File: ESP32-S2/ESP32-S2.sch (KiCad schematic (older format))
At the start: 39 parts, among them J1 Conn_01x21_Male, J2 Conn_01x21_Male, J21 USB-C, Q1 L8050QLT1G, Q2 L8050QLT1G, SW1 BOOT/SELECT, SW2 EN/RESET, U1 ESP32-S2-WROOM, U2 SSD1306, U3 ATECC608A-SSHDA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

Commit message: resolved errors
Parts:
- C10, C9: value CP -> 1uF
- C11: value C_Small -> 10uF
- C6: value C_Small -> 1uF
- C7: value C_Small -> 0.1uF
- C8: value C_Small -> 2uF
- R5: value R_Small_US -> 390K
- R8: value R -> 4.7K
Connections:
- net labels added: VDD33, ~CTS, ~DTR
- net labels removed: CTS', DTR, DTR', Text Label 7420 2020 1    50   ~ 0
- wire segments 299 -> 286
- no-connect marks 6 -> 9
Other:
- moved on the sheet: C10, C9, R10, R6

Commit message: Some Changes in Schematic
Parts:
- removed U3: ATECC608A-SSHDA, Package_SO:SOIC-8_3.9x4.9mm_P1.27mm, symbol Security:ATECC608A-SSHDA
- added C9: C_Small, Capacitor_SMD:C_1206_3216Metric, symbol Device:C_Small
- added D4: 1N5819, Diode_THT:D_DO-41_SOD81_P10.16mm_Horizontal, symbol Diode:1N5819
- added J3: USB_A, symbol Connector:USB_A
- added Q1: DMP3013SFV, Package_SON:Diodes_PowerDI3333-8, symbol Transistor_FET:DMP3013SFV
- added R10: 220, Resistor_SMD:R_0603_1608Metric, symbol Device:R_Small_US
- added R11, R5, R8: 10K, Resistor_SMD:R_0603_1608Metric, symbol Device:R
- added R9: 100, Resistor_SMD:R_0603_1608Metric, symbol Device:R_Small_US
- added U3: LM1117-3.3, symbol Regulator_Linear:LM1117-3.3
- C1: renamed from C4; footprint (none) -> Capacitor_SMD:C_1206_3216Metric
- C10: renamed from C3; footprint (none) -> Capacitor_SMD:C_1206_3216Metric
- C11: renamed from C1; footprint (none) -> Capacitor_SMD:C_1206_3216Metric
- C12, C13, C5: footprint (none) -> Capacitor_SMD:C_1206_3216Metric
- C14: renamed from C2; footprint (none) -> Capacitor_SMD:C_1206_3216Metric
- C2: renamed from C6; footprint (none) -> Capacitor_SMD:C_1206_3216Metric
- C3: renamed from C7; footprint (none) -> Capacitor_SMD:C_1206_3216Metric
- C4: renamed from C8; footprint (none) -> Capacitor_SMD:C_1206_3216Metric
- C6: renamed from C9; footprint (none) -> Capacitor_SMD:C_1206_3216Metric
- C7: renamed from C10; footprint (none) -> Capacitor_SMD:C_1206_3216Metric
- C8: renamed from C11; footprint (none) -> Capacitor_SMD:C_1206_3216Metric
- D2, D3: footprint (none) -> LED_SMD:LED_0603_1608Metric_Castellated
- J2: footprint Connector_PinHeader_2.00mm:PinHeader_1x07_P2.00mm_Vertical -> Connector_PinHeader_2.00mm:PinHeader_1x21_P2.00mm_Vertical
- Q2: renamed from Q1; footprint (none) -> Button_Switch_SMD:SW_Push_1P1T_NO_6x6mm_H9.5mm
- Q3: renamed from Q2; footprint (none) -> Button_Switch_SMD:SW_Push_1P1T_NO_6x6mm_H9.5mm
- R1: renamed from R5; footprint (none) -> Resistor_SMD:R_0603_1608Metric
- R12: renamed from R9; footprint (none) -> Resistor_SMD:R_0603_1608Metric
- R13: renamed from R10; footprint (none) -> Resistor_SMD:R_0603_1608Metric
- R14: renamed from R3; footprint (none) -> Resistor_SMD:R_0603_1608Metric
- R15: renamed from R1; footprint (none) -> Resistor_SMD:R_0603_1608Metric
- R16: renamed from R2; footprint (none) -> Resistor_SMD:R_0603_1608Metric
- R17: renamed from R4; footprint (none) -> Resistor_SMD:R_0603_1608Metric
- R2: renamed from R6; footprint (none) -> Resistor_SMD:R_0603_1608Metric
- R3: renamed from R7; footprint (none) -> Resistor_SMD:R_0603_1608Metric
- R4: renamed from R8; footprint (none) -> Resistor_SMD:R_0603_1608Metric
- R6: renamed from R11; footprint (none) -> Resistor_SMD:R_0603_1608Metric
- R7: renamed from R12; footprint (none) -> Resistor_SMD:R_0603_1608Metric
- U2: renamed from U1; footprint XCVR_ESP32-S2-WROOM -> RF_Module:ESP32-WROOM-32
- renumbered J21 to J4, SW2 to SW1, SW1 to SW2, U2 to U1
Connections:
- net labels added: +BATT, VBUS, ~RTS
- net labels removed: RTS, SHLD, ~CTS
- wire segments 286 -> 320
- no-connect marks 9 -> 7
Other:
- moved on the sheet: C10, C11, C12, C13, C14, D2, D3, J4, Q2, Q3, R12, R13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

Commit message: made suggested changes
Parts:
- removed U3: LM1117-3.3, symbol Regulator_Linear:LM1117-3.3
- added TP1: GND, symbol Connector:TestPoint
- added TP2: 3V3, symbol Connector:TestPoint
- added TP3: SCL, symbol Connector:TestPoint
- added TP4: SDA, symbol Connector:TestPoint
- added U3: AMS1117-3.3, Package_TO_SOT_SMD:SOT-223-3_TabPin2, symbol Regulator_Linear:AMS1117-3.3
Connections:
- net +3V3: now also TP2.1, U3.2 (VO)
- net GND: now also TP1.1
- net SCL: now also R2.1, TP3.1; no longer R3.1
- net SDA: now also R3.1, TP4.1; no longer R2.1
- net RES#: now reaches C8.1, D1.2 (A), R4.2, U1.14 (RES#)
- net at D4.2 (A), Q1.1 (S), Q1.2 (S)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: now also U3.3 (VI)
- net at R10.1, R9.2: now also U3.1 (GND)
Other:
- note added: "Test Points\n"
- note added: "USB-A Voltage Divider\n\n"
- note added: "USB-C to UART\n"
- note removed: "USB and CH340C"
- note removed: "Voltage Divider\n"
- moved on the sheet: C10, C11, C8, C9, D1, D4, J2, Q1, R10, R11, R2, R3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

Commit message: Made changes in schematics
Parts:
- removed C9: C_Small, Capacitor_SMD:C_1206_3216Metric, symbol Device:C_Small
- removed R10: 220, Resistor_SMD:R_0603_1608Metric, symbol Device:R_Small_US
- removed R9: 100, Resistor_SMD:R_0603_1608Metric, symbol Device:R_Small_US
- removed U3: AMS1117-3.3, Package_TO_SOT_SMD:SOT-223-3_TabPin2, symbol Regulator_Linear:AMS1117-3.3
- added C15, C9, C?: 10uF, symbol Device:C
- added C?: 0.1uF, symbol Device:C
- added L1: 2.2uH, symbol Device:L
- added R?: R, symbol Device:R
- added U3: TPS63001, Package_SON:Texas_DRC0010J_ThermalVias, symbol Regulator_Switching:TPS63001
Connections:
- net GND: now also C15.2, C9.2, C?.2, C?.2, U3.11 (PGND), U3.3 (PGND), U3.9 (GND)
- new net: C15.1, C?.1, U3.1 (VOUT), U3.10 (FB)
- new net: L1.2, U3.2 (L2)
- new net: L1.1, U3.4 (L1)
- new net: R?.1, U3.5 (VIN)
- new net: C?.1, R?.2, U3.6 (EN), U3.7 (PS/SYNC), U3.8 (VINA)

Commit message: minor changes
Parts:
- R9: renamed from R?; value R -> 100
- gave numbers to parts that had none: 2
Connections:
- net +3V3: now also C15.1, C17.1, U3.1 (VOUT), U3.10 (FB)
- net at C9.1: now also D4.2 (A), Q1.1 (S), Q1.2 (S), Q1.3 (S)
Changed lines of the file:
@@
 Wire Notes Line
 	6970 7790 6970 5880
-Wire Notes Line
-	500  5880 6970 5880
 Text Notes 1325 725  0    93   ~ 0
 RF-Module
@@
 Wire Notes Line
 	2815 4060 2815 5905
-Wire Notes Line
-	2815 5905 2765 5905
 Wire Wire Line
 	2975 5130 2975 5225
@@
 	1    4660 5245
 	1    0    0    -1
-$EndComp
-$Comp
-L Device:R R11
-U 1 1 60557FF9
-P 4340 5505
-F 0 "R11" V 4430 5460 50  0000 L CNN
-F 1 "10K" V 4240 5435 50  0000 L CNN
-F 2 "Resistor_SMD:R_0603_1608Metric" V 4270 5505 50  0001 C CNN
-F 3 "~" H 4340 5505 50  0001 C CNN
-	1    4340 5505
-	-1   0    0    1
 $EndComp
 $Comp
@@
 Wire Notes Line
 	2095 7800 4370 7800
-Text Notes 3020 4430 0    118  ~ 0
-USB-A          Voltage Divider\n\n
-$Comp
-L Regulator_Switching:TPS63001 U3
-U 1 1 602467D8
-P 6300 4900
-F 0 "U3" H 6300 5567 50  0000 C CNN
-F 1 "TPS63001" H 6300 5476 50  0000 C CNN
-F 2 "Package_SON:Texas_DRC0010J_ThermalVias" H 7150 4350 50  0001 C CNN
-F 3 "http://www.ti.com/lit/ds/symlink/tps63000.pdf" H 6000 5450 50  0001 C CNN
-	1    6300 4900
-	1    0    0    -1
-$EndComp
-$Comp
-L Device:C C15
-U 1 1 6024B0B6
-P 6900 4950
-F 0 "C15" H 7015 4996 50  0000 L CNN
-F 1 "10uF" H 7015 4905 50  0000 L CNN
-F 2 "" H 6938 4800 50  0001 C CNN
-F 3 "~" H 6900 4950 50  0001 C CNN
-	1    6900 4950
-	1    0    0    -1
-$EndComp
-$Comp
-L Device:L L1
-U 1 1 6024B4E6
-P 6250 4200
-F 0 "L1" V 6440 4200 50  0000 C CNN
-F 1 "2.2uH" V 6349 4200 50  0000 C CNN
-F 2 "" H 6250 4200 50  0001 C CNN
-F 3 "~" H 6250 4200 50  0001 C CNN
-	1    6250 4200
-	0    -1   -1   0
-$EndComp
-Wire Wire Line
-	6100 4200 5800 4200
-Wire Wire Line
-	5800 4200 5800 4500
-Wire Wire Line
-	5800 4500 5900 4500
-Wire Wire Line
-	6400 4200 6850 4200
-Wire Wire Line
-	6850 4500 6700 4500
-Wire Wire Line
-	6850 4200 6850 4500
-$Comp
-L Device:C C9
-U 1 1 6024A509
-P 5650 5550
-F 0 "C9" H 5765 5596 50  0000 L CNN
-F 1 "10uF" H 5765 5505 50  0000 L CNN
-F 2 "" H 5688 5400 50  0001 C CNN
-F 3 "~" H 5650 5550 50  0001 C CNN
-	1    5650 5550
-	1    0    0    -1
-$EndComp
-Wire Wire Line
-	9150 3100 9250 3100
 Wire Notes Line
 	7450 5900 6950 5900
-Wire Wire Line
-	5650 5400 5650 5250
-Wire Wire Line
-	6700 4700 6750 4700
-Wire Wire Line
-	7200 5100 7200 5700
-Wire Wire Line
-	7200 5700 6900 5700
-Wire Wire Line
-	6900 5100 6900 5700
-Connection ~ 6900 5700
-Wire Wire Line
-	6900 5700 6550 5700
-Wire Wire Line
-	6200 5500 6200 5700
-Connection ~ 6200 5700
-Wire Wire Line
-	6200 5700 5800 5700
-Wire Wire Line
-	6300 5500 6300 5700
-Connection ~ 6300 5700
-Wire Wire Line
-	6300 5700 6200 5700
-Wire Wire Line
-	5000 5250 5650 5250
-Wire Wire Line
-	6700 4900 6750 4900
-Wire Wire Line
-	6750 4900 6750 4700
-Connection ~ 6750 4700
-Wire Wire Line
-	6750 4700 6900 4700
 $Comp
 L power:+3.3V #PWR011
@@
 	0    -1   -1   0
 $EndComp
-Wire Wire Line
-	6900 4700 6900 4800
-$Comp
-L Device:C C?
+Wire Notes Line
+	7450 4050 7450 5900
+Wire Notes Line
+	505  5905 6975 5905
+$Comp
+L Device:R R11
+U 1 1 60557FF9
+P 4340 5505
+F 0 "R11" H 4405 5435 50  0000 L CNN
+F 1 "10K" H 4410 5545 50  0000 L CNN
+F 2 "Resistor_SMD:R_0603_1608Metric" V 4270 5505 50  0001 C CNN
+F 3 "~" H 4340 5505 50  0001 C CNN
+	1    4340 5505
+	-1   0    0    1
+$EndComp
+Connection ~ 7200 4700
+Wire Wire Line
+	6900 4700 7200 4700
+$Comp
+L power:+3.3V #PWR030
+U 1 1 60EFC8D8
+P 7200 4700
+F 0 "#PWR030" H 7200 4550 50  0001 C CNN
+F 1 "+3.3V" H 7215 4873 50  0000 C CNN
+F 2 "" H 7200 4700 50  0001 C CNN
+F 3 "" H 7200 4700 50  0001 C CNN
+	1    7200 4700
+	1    0    0    -1
+$EndComp
+Wire Wire Line
+	5900 4900 5900 5100
+Connection ~ 5900 4900
+Connection ~ 5900 5100
+Wire Wire Line
+	5900 4800 5900 4900
+Wire Wire Line
+	5800 5100 5800 5150
+Connection ~ 5800 5100
+Wire Wire Line
+	5900 5100 5800 5100
+Wire Wire Line
+	5800 5700 5650 5700
+Connection ~ 5800 5700
+Wire Wire Line
+	5800 5450 5800 5700
+Wire Wire Line
+	5800 5050 5800 5100
+Wire Wire Line
+	5800 4700 5800 4750
+Wire Wire Line
+	5900 4700 5800 4700
+Connection ~ 6900 4700
+Wire Wire Line
+	7200 4700 7200 4800
+$Comp
+L Device:R R9
+U 1 1 60DDB77B
+P 5800 4900
+F 0 "R9" H 5650 4965 50  0000 L CNN
+F 1 "100" H 5610 4870 50  0000 L CNN
+F 2 "" V 5730 4900 50  0001 C CNN
+F 3 "~" H 5800 4900 50  0001 C CNN
+	1    5800 4900
+	1    0    0    -1
+$EndComp
+Wire Wire Line
+	6550 5700 6300 5700
+Connection ~ 6550 5700
+$Comp
+L power:GND #PWR025
+U 1 1 60D216C3
+P 6550 5700
+F 0 "#PWR025" H 6550 5450 50  0001 C CNN
+F 1 "GND" H 6550 5550 50  0000 C CNN
+F 2 "" H 6550 5700 50  0001 C CNN
+F 3 "" H 6550 5700 50  0001 C CNN
+	1    6550 5700
+	1    0    0    -1
+$EndComp
+$Comp
+L Device:C C17
+U 1 1 60D210CD
+P 7200 4950
+F 0 "C17" H 7270 5040 50  0000 L CNN
+F 1 "10uF" H 7255 4860 50  0000 L CNN
+F 2 "" H 7238 4800 50  0001 C CNN
+F 3 "~" H 7200 4950 50  0001 C CNN
+	1    7200 4950
+	1    0    0    -1
+$EndComp
+$Comp
+L Device:C C16
 U 1 1 60D204A0
 P 5800 5300
-F 0 "C?" H 5915 5346 50  0000 L CNN
-F 1 "0.1uF" H 5915 5255 50  0000 L CNN
+F 0 "C16" H 5835 5395 50  0000 L CNN
+F 1 "0.1uF" H 5795 5220 50  0000 L CNN
 F 2 "" H 5838 5150 50  0001 C CNN
 F 3 "~" H 5800 5300 50  0001 C CNN
@@
 	1    0    0    -1
 $EndComp
-$Comp
-L Device:C C?
-U 1 1 60D210CD
-P 7200 4950
-F 0 "C?" H 7315 4996 50  0000 L CNN
-F 1 "10uF" H 7315 4905 50  0000 L CNN
-F 2 "" H 7238 4800 50  0001 C CNN
-F 3 "~" H 7200 4950 50  0001 C CNN
-	1    7200 4950
-	1    0    0    -1
-$EndComp
-$Comp
-L power:GND #PWR?
-U 1 1 60D216C3
-P 6550 5700
-F 0 "#PWR?" H 6550 5450 50  0001 C CNN
-F 1 "GND" H 6555 5527 50  0000 C CNN
-F 2 "" H 6550 5700 50  0001 C CNN
-F 3 "" H 6550 5700 50  0001 C CNN
-	1    6550 5700
-	1    0    0    -1
-$EndComp
-Connection ~ 6550 5700
-Wire Wire Line
-	6550 5700 6300 5700
-$Comp
-L Device:R R?
-U 1 1 60DDB77B
-P 5800 4900
-F 0 "R?" H 5870 4946 50  0000 L CNN
-F 1 "R" H 5870 4855 50  0000 L CNN
-F 2 "" V 5730 4900 50  0001 C CNN
-F 3 "~" H 5800 4900 50  0001 C CNN
-	1    5800 4900
-	1    0    0    -1
-$EndComp
-Wire Wire Line
-	7200 4700 7200 4800
-Connection ~ 6900 4700
-Wire Wire Line
-	5900 4700 5800 4700
-Wire Wire Line
-	5800 4700 5800 4750
-Wire Wire Line
-	5800 5050 5800 5100
-Wire Wire Line
-	5800 5450 5800 5700
-Connection ~ 5800 5700
-Wire Wire Line
-	5800 5700 5650 5700
-Wire Wire Line
-	5900 5100 5800 5100
-Connection ~ 5800 5100
-Wire Wire Line
-	5800 5100 5800 5150
-Wire Wire Line
-	5900 4800 5900 4900
-Connection ~ 5900 5100
-Connection ~ 5900 4900
-Wire Wire Line
-	5900 4900 5900 5100
-Wire Notes Line
-	7450 4050 7450 5900
-$Comp
-L power:+3.3V #PWR?
-U 1 1 60EFC8D8
-P 7135 4670
-F 0 "#PWR?" H 7135 4520 50  0001 C CNN
-F 1 "+3.3V" H 7150 4843 50  0000 C CNN
-F 2 "" H 7135 4670 50  0001 C CNN
-F 3 "" H 7135 4670 50  0001 C CNN
-	1    7135 4670
-	1    0    0    -1
-$EndComp
-Wire Wire Line
-	6900 4700 7200 4700
+Wire Wire Line
+	6900 4700 6900 4800
+Wire Wire Line
+	6750 4700 6900 4700
+Connection ~ 6750 4700
+Wire Wire Line
+	6750 4900 6750 4700
+Wire Wire Line
+	6700 4900 6750 4900
+Wire Wire Line
+	6300 5700 6200 5700
+Connection ~ 6300 5700
+Wire Wire Line
+	6300 5500 6300 5700
+Wire Wire Line
+	6200 5700 5800 5700
+Connection ~ 6200 5700
+Wire Wire Line
+	6200 5500 6200 5700
+Wire Wire Line
+	6900 5700 6550 5700
+Connection ~ 6900 5700
+Wire Wire Line
+	6900 5100 6900 5700
+Wire Wire Line
+	7200 5700 6900 5700
+Wire Wire Line
+	7200 5100 7200 5700
+Wire Wire Line
+	6700 4700 6750 4700
+Wire Wire Line
+	5650 5400 5650 5250
+$Comp
+L Device:C C9
+U 1 1 6024A509
+P 5650 5550
+F 0 "C9" H 5495 5645 50  0000 L CNN
+F 1 "10uF" H 5430 5465 50  0000 L CNN
+F 2 "" H 5688 5400 50  0001 C CNN
+F 3 "~" H 5650 5550 50  0001 C CNN
+	1    5650 5550
+	1    0    0    -1
+$EndComp
+Wire Wire Line
+	6850 4200 6850 4500
+Wire Wire Line
+	6850 4500 6700 4500
+Wire Wire Line
+	6400 4200 6850 4200
+Wire Wire Line
+	5800 4500 5900 4500
+Wire Wire Line
+	6100 4200 5800 4200
+$Comp
+L Device:L L1
+U 1 1 6024B4E6
+P 6250 4200
+F 0 "L1" V 6325 4285 50  0000 C CNN
+F 1 "2.2uH" V 6315 4055 50  0000 C CNN
+F 2 "" H 6250 4200 50  0001 C CNN
+F 3 "~" H 6250 4200 50  0001 C CNN
+	1    6250 4200
+	0    -1   -1   0
+$EndComp
+$Comp
+L Device:C C15
+U 1 1 6024B0B6
+P 6900 4950
+F 0 "C15" H 6955 5040 50  0000 L CNN
+F 1 "10uF" H 6940 4870 50  0000 L CNN
+F 2 "" H 6938 4800 50  0001 C CNN
+F 3 "~" H 6900 4950 50  0001 C CNN
+	1    6900 4950
+	1    0    0    -1
+$EndComp
+$Comp
+L Regulator_Switching:TPS63001 U3
+U 1 1 602467D8
+P 6300 4900
+F 0 "U3" H 6300 5567 50  0000 C CNN
+F 1 "TPS63001" H 6300 5476 50  0000 C CNN
+F 2 "Package_SON:Texas_DRC0010J_ThermalVias" H 7150 4350 50  0001 C CNN
+F 3 "http://www.ti.com/lit/ds/symlink/tps63000.pdf" H 6000 5450 50  0001 C CNN
+	1    6300 4900
+	1    0    0    -1
+$EndComp
+Wire Wire Line
+	5800 4200 5800 4500
+Text Notes 2915 4420 0    118  ~ 0
+USB-A          Voltage Divider\n\n
+Wire Wire Line
+	5650 5250 5010 5250
+Wire Wire Line
+	5010 5250 5010 5245
+Connection ~ 5010 5245
 $EndSCHEMATC

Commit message: Changes in Schematic
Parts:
- removed D4: 1N5819, Diode_THT:D_DO-41_SOD81_P10.16mm_Horizontal, symbol Diode:1N5819
- removed J1: Conn_01x21_Male, Connector_PinHeader_2.00mm:PinHeader_1x21_P2.00mm_Vertical, symbol Connector:Conn_01x21_Male
- removed Q1: DMP3013SFV, Package_SON:Diodes_PowerDI3333-8, symbol Transistor_FET:DMP3013SFV
- removed R11: 10K, Resistor_SMD:R_0603_1608Metric, symbol Device:R
- added J1: Conn_01x15_Male, Connector_PinHeader_2.00mm:PinHeader_1x16_P2.00mm_Vertical, symbol Connector:Conn_01x16_Male
- C15, C16, C17, C9: footprint (none) -> Capacitor_SMD:C_1206_3216Metric
- J2: value Conn_01x21_Male -> Conn_01x16_Male; footprint Connector_PinHeader_2.00mm:PinHeader_1x21_P2.00mm_Vertical -> Connector_PinHeader_2.00mm:PinHeader_1x16_P2.00mm_Vertical; symbol Connector:Conn_01x21_Male -> Connector:Conn_01x16_Male
- L1: footprint (none) -> Inductor_SMD:L_0201_0603Metric
- R9: footprint (none) -> Resistor_SMD:R_0603_1608Metric
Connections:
- net CHIP_PU: no longer J2.2 (Pin_2)
- net GND: now also J1.1 (Pin_1); no longer J2.1 (Pin_1), J3.2 (D-), J3.3 (D+)
- net GPIO1: now also J1.2 (Pin_2)
- net GPIO10: now also J1.11 (Pin_11)
- net GPIO11: now also J1.12 (Pin_12)
- net GPIO12: now also J1.13 (Pin_13)
- net GPIO13: now also J1.14 (Pin_14)
- net GPIO14: now also J1.15 (Pin_15)
- net GPIO15: now also J1.16 (Pin_16)
- net GPIO16: now also J2.1 (Pin_1)
- net GPIO17: now also J2.2 (Pin_2)
- net GPIO19: now also J3.2 (D-); no longer J2.20 (Pin_20)
- net GPIO2: now also J1.3 (Pin_3)
- net GPIO20: now also J2.3 (Pin_3), J3.3 (D+); no longer J2.19 (Pin_19)
- net GPIO21: now also J2.4 (Pin_4); no longer J2.18 (Pin_18)
- net GPIO26: now also J2.5 (Pin_5); no longer J2.17 (Pin_17)
- net GPIO3: now also J1.4 (Pin_4)
- net GPIO33: now also J2.6 (Pin_6); no longer J2.16 (Pin_16)
- net GPIO34: now also J2.7 (Pin_7); no longer J2.15 (Pin_15)
- net GPIO35: now also J2.8 (Pin_8); no longer J2.14 (Pin_14)
- net GPIO36: now also J2.9 (Pin_9); no longer J2.13 (Pin_13)
- net GPIO37: now also J2.10 (Pin_10); no longer J2.12 (Pin_12)
- net GPIO39: now also J2.12 (Pin_12); no longer J2.10 (Pin_10)
- net GPIO4: now also J1.5 (Pin_5)
- net GPIO42: now also J2.13 (Pin_13); no longer J2.7 (Pin_7)
- net GPIO45: now also J2.14 (Pin_14); no longer J2.4 (Pin_4)
- net GPIO46: now also J2.15 (Pin_15); no longer J2.3 (Pin_3)
- net GPIO5: now also J1.6 (Pin_6)
- net GPIO6: now also J1.7 (Pin_7)
- net GPIO7: now also J1.8 (Pin_8)
- net GPIO8: now also J1.9 (Pin_9)
- net GPIO9: now also J1.10 (Pin_10)
- net RXD0: no longer J2.5 (Pin_5), J2.9 (Pin_9)
- net TXD0: no longer J2.6 (Pin_6), J2.8 (Pin_8)
- net VBUS: now also C9.1
- net VCC: now also J2.16 (Pin_16)
- removed net EXT_GPIO18: J2.21 (Pin_21)
- no-connect marks 7 -> 6
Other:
- note removed: "USB-A Voltage Divider\n\n"

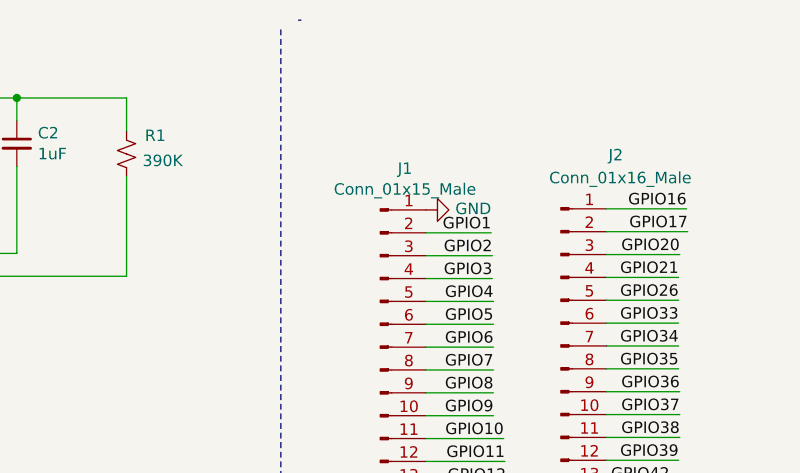
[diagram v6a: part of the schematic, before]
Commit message: added footprints
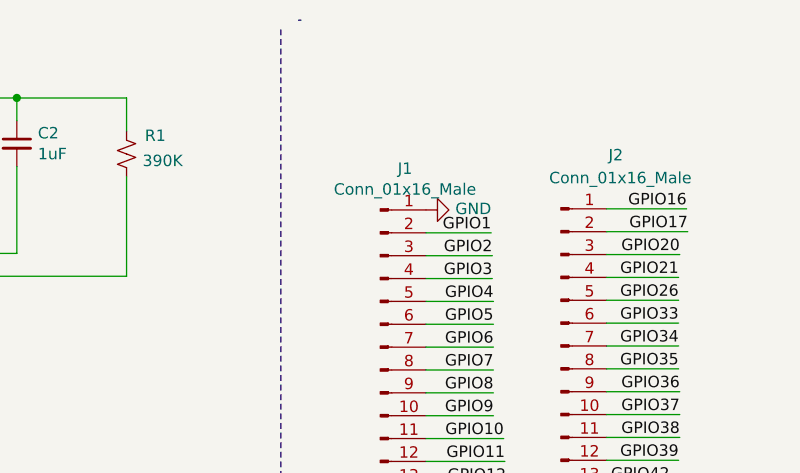
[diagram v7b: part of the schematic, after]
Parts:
- J1: value Conn_01x15_Male -> Conn_01x16_Male
- J4: footprint (none) -> TYPE-C-31-M-17:TYPEC31M17
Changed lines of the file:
@@
 F 0 "J4" H 7855 5440 50  0000 C CNN
 F 1 "USB-C" H 7855 4620 50  0000 C CNN
-F 2 "" H 7755 5435 50  0001 C CNN
+F 2 "TYPE-C-31-M-17:TYPEC31M17" H 7755 5435 50  0001 C CNN
 F 3 "" H 7755 5435 50  0001 C CNN
 	1    7805 5285
@@
 P 9470 1985
 F 0 "J1" H 9578 2866 50  0000 C CNN
-F 1 "Conn_01x15_Male" H 9578 2775 50  0000 C CNN
+F 1 "Conn_01x16_Male" H 9578 2775 50  0000 C CNN
 F 2 "Connector_PinHeader_2.00mm:PinHeader_1x16_P2.00mm_Vertical" H 9470 1985 50  0001 C CNN
 F 3 "~" H 9470 1985 50  0001 C CNN

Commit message: Started Routing
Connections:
- no-connect marks 6 -> 11
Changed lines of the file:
@@
 L power:GND #PWR05
 U 1 1 60579A17
-P 9670 1285
-F 0 "#PWR05" H 9670 1035 50  0001 C CNN
-F 1 "GND" V 9675 1157 50  0000 R CNN
-F 2 "" H 9670 1285 50  0001 C CNN
-F 3 "" H 9670 1285 50  0001 C CNN
-	1    9670 1285
+P 9730 1285
+F 0 "#PWR05" H 9730 1035 50  0001 C CNN
+F 1 "GND" V 9735 1157 50  0000 R CNN
+F 2 "" H 9730 1285 50  0001 C CNN
+F 3 "" H 9730 1285 50  0001 C CNN
+	1    9730 1285
 	0    -1   -1   0
 $EndComp
@@
 	1    0    0    -1
 $EndComp
+NoConn ~ 2710 1890
+NoConn ~ 2715 1995
+NoConn ~ 10100 1115
+Wire Wire Line
+	9670 1285 9730 1285
+NoConn ~ 2365 1890
+NoConn ~ 2360 1990
 $EndSCHEMATC
